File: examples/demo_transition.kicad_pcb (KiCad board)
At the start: 4 copper layers, 20 x 10 mm, 2 parts

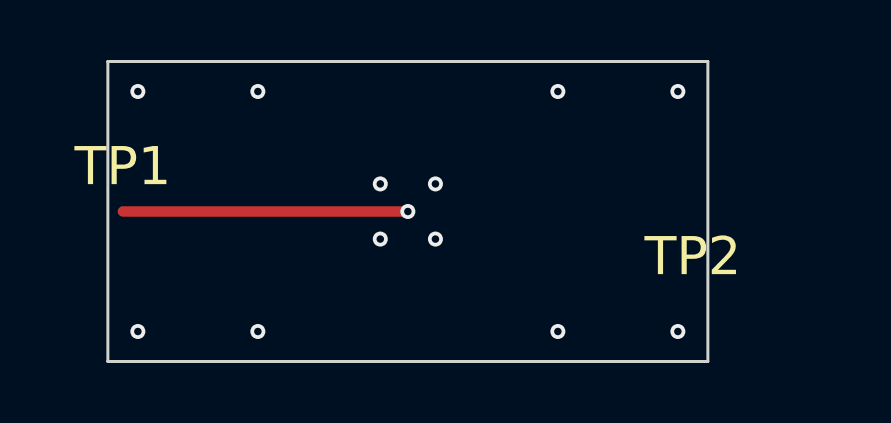
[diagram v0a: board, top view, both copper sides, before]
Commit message: KiCad workflow: CLI, port impedance characterisation, mesher robustness, direct solver
- mom25d_cli: .kicad_pcb / .gbrjob -> Touchstone + dashboard + JSON summary,
  adaptive sweep, TOML config, per-layer mesh controls
- BoardModel.characterize: wave-port reference impedance from the port's
  cross-section (trace + covering metal), interpolated over frequency
- wave-port sample cuts spread over the usable feed (low-frequency conditioning)
- mesher: snap-rounding noding (T-junctions), KD-tree vertex merge, regional
  area limits refining planes under nearby traces
- 'direct' solver: dense LU of the fast-operator entries (memory ~ Z only);
  'auto' solver choice; symmetric equilibration in all direct solves
- demo board: via fence along the stripline; examples/demo_transition.mom25d.toml
- tests/test_stage3.py: vias vs exact images, off-plane integrals, mesher
  T-junctions, lumped elements, via ports, AAA, KiCad + Gerber import,
  fast/direct/ACA vs dense

Co-Authored-By: Claude Opus 5.5 <noreply@anthropic.com>
Claude-Session: https://claude.ai/code/session_01RgVFvps66y9W41KBD85DuR
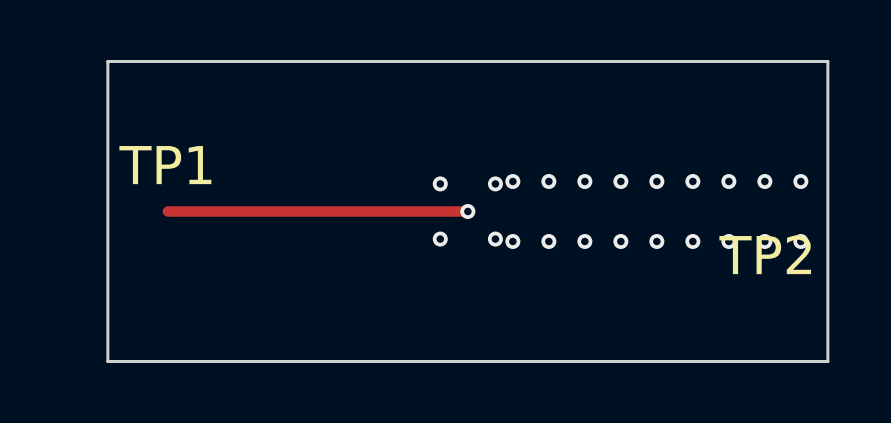
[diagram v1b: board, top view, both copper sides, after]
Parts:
- moved TP2 2.50 mm to (22.0, 5.00)
- moved TP1 1.50 mm to (2.00, 5.00)
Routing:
- net RF: track 19.0 -> 20.0 mm
- net GND: vias 12 -> 22
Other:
- board size 20 x 10 mm -> 24 x 10 mm
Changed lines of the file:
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@@
     (pad_to_mask_clearance 0))
   (net 0 "") (net 1 "GND") (net 2 "RF")
-  (segment (start 0.5 5.0) (end 10.0 5.0) (width 0.35) (layer "F.Cu") (net 2))
-  (segment (start 10.0 5.0) (end 19.5 5.0) (width 0.15) (layer "In2.Cu") (net 2))
-  (via blind (at 10.0 5.0) (size 0.5) (drill 0.25) (layers "F.Cu" "In2.Cu") (net 2))
-  (via (at 10.9192 5.9192) (size 0.5) (drill 0.25) (layers "F.Cu" "B.Cu") (net 1))
-  (via (at 9.0808 5.9192) (size 0.5) (drill 0.25) (layers "F.Cu" "B.Cu") (net 1))
-  (via (at 9.0808 4.0808) (size 0.5) (drill 0.25) (layers "F.Cu" "B.Cu") (net 1))
-  (via (at 10.9192 4.0808) (size 0.5) (drill 0.25) (layers "F.Cu" "B.Cu") (net 1))
-  (via (at 1.0000 1.0000) (size 0.5) (drill 0.25) (layers "F.Cu" "B.Cu") (net 1))
-  (via (at 1.0000 9.0000) (size 0.5) (drill 0.25) (layers "F.Cu" "B.Cu") (net 1))
-  (via (at 5.0000 1.0000) (size 0.5) (drill 0.25) (layers "F.Cu" "B.Cu") (net 1))
-  (via (at 5.0000 9.0000) (size 0.5) (drill 0.25) (layers "F.Cu" "B.Cu") (net 1))
-  (via (at 15.0000 1.0000) (size 0.5) (drill 0.25) (layers "F.Cu" "B.Cu") (net 1))
-  (via (at 15.0000 9.0000) (size 0.5) (drill 0.25) (layers "F.Cu" "B.Cu") (net 1))
-  (via (at 19.0000 1.0000) (size 0.5) (drill 0.25) (layers "F.Cu" "B.Cu") (net 1))
-  (via (at 19.0000 9.0000) (size 0.5) (drill 0.25) (layers "F.Cu" "B.Cu") (net 1))
+  (segment (start 2.0 5.0) (end 12.0 5.0) (width 0.35) (layer "F.Cu") (net 2))
+  (segment (start 12.0 5.0) (end 22.0 5.0) (width 0.15) (layer "In2.Cu") (net 2))
+  (via blind (at 12.0 5.0) (size 0.5) (drill 0.25) (layers "F.Cu" "In2.Cu") (net 2))
+  (via (at 12.9192 5.9192) (size 0.5) (drill 0.25) (layers "F.Cu" "B.Cu") (net 1))
+  (via (at 11.0808 5.9192) (size 0.5) (drill 0.25) (layers "F.Cu" "B.Cu") (net 1))
+  (via (at 11.0808 4.0808) (size 0.5) (drill 0.25) (layers "F.Cu" "B.Cu") (net 1))
+  (via (at 12.9192 4.0808) (size 0.5) (drill 0.25) (layers "F.Cu" "B.Cu") (net 1))
+  (via (at 13.5000 4.0000) (size 0.5) (drill 0.25) (layers "F.Cu" "B.Cu") (net 1))
+  (via (at 13.5000 6.0000) (size 0.5) (drill 0.25) (layers "F.Cu" "B.Cu") (net 1))
+  (via (at 14.7000 4.0000) (size 0.5) (drill 0.25) (layers "F.Cu" "B.Cu") (net 1))
+  (via (at 14.7000 6.0000) (size 0.5) (drill 0.25) (layers "F.Cu" "B.Cu") (net 1))
+  (via (at 15.9000 4.0000) (size 0.5) (drill 0.25) (layers "F.Cu" "B.Cu") (net 1))
+  (via (at 15.9000 6.0000) (size 0.5) (drill 0.25) (layers "F.Cu" "B.Cu") (net 1))
+  (via (at 17.1000 4.0000) (size 0.5) (drill 0.25) (layers "F.Cu" "B.Cu") (net 1))
+  (via (at 17.1000 6.0000) (size 0.5) (drill 0.25) (layers "F.Cu" "B.Cu") (net 1))
+  (via (at 18.3000 4.0000) (size 0.5) (drill 0.25) (layers "F.Cu" "B.Cu") (net 1))
+  (via (at 18.3000 6.0000) (size 0.5) (drill 0.25) (layers "F.Cu" "B.Cu") (net 1))
+  (via (at 19.5000 4.0000) (size 0.5) (drill 0.25) (layers "F.Cu" "B.Cu") (net 1))
+  (via (at 19.5000 6.0000) (size 0.5) (drill 0.25) (layers "F.Cu" "B.Cu") (net 1))
+  (via (at 20.7000 4.0000) (size 0.5) (drill 0.25) (layers "F.Cu" "B.Cu") (net 1))
+  (via (at 20.7000 6.0000) (size 0.5) (drill 0.25) (layers "F.Cu" "B.Cu") (net 1))
+  (via (at 21.9000 4.0000) (size 0.5) (drill 0.25) (layers "F.Cu" "B.Cu") (net 1))
+  (via (at 21.9000 6.0000) (size 0.5) (drill 0.25) (layers "F.Cu" "B.Cu") (net 1))
+  (via (at 23.1000 4.0000) (size 0.5) (drill 0.25) (layers "F.Cu" "B.Cu") (net 1))
+  (via (at 23.1000 6.0000) (size 0.5) (drill 0.25) (layers "F.Cu" "B.Cu") (net 1))
   (zone (net 1) (net_name "GND") (layer "In1.Cu") (hatch edge 0.5)
     (connect_pads (clearance 0.2)) (min_thickness 0.2) (filled_areas_thickness no)
     (fill yes (thermal_gap 0.5) (thermal_bridge_width 0.5))
-    (polygon (pts (xy 0 0) (xy 20.0 0) (xy 20.0 10.0) (xy 0 10.0)))
-  (footprint "mom25d:RF_Port" (layer "F.Cu") (at 0.5 5.0 0)
+    (polygon (pts (xy 0 0) (xy 24.0 0) (xy 24.0 10.0) (xy 0 10.0)))
+  (footprint "mom25d:RF_Port" (layer "F.Cu") (at 2.0 5.0 0)
     (property "Reference" "TP1" (at 0 -1.5 0) (layer "F.SilkS"))
     (property "Value" "RF_Port" (at 0 1.5 0) (layer "F.Fab"))
@@
     (fp_line (start -0.5 0) (end 0.5 0) (stroke (width 0.1) (type solid)) (layer "F.Fab"))
   )
-  (footprint "mom25d:RF_Port" (layer "F.Cu") (at 19.5 5.0 180)
+  (footprint "mom25d:RF_Port" (layer "F.Cu") (at 22.0 5.0 180)
     (property "Reference" "TP2" (at 0 -1.5 180) (layer "F.SilkS"))
     (property "Value" "RF_Port" (at 0 1.5 180) (layer "F.Fab"))
@@
     (fp_line (start -0.5 0) (end 0.5 0) (stroke (width 0.1) (type solid)) (layer "F.Fab"))
   )
-  (gr_rect (start 0 0) (end 20.0 10.0) (stroke (width 0.1) (type default)) (fill none) (layer "Edge.Cuts"))
+  (gr_rect (start 0 0) (end 24.0 10.0) (stroke (width 0.1) (type default)) (fill none) (layer "Edge.Cuts"))
 )
